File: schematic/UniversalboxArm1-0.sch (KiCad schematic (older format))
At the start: 170 parts, among them J1 USB_B_Micro, J110 Conn_01x03_Male, J120 Conn_02x04_Counter_Clockwise, J121 Conn_01x02_Male, J20 AVR-ISP-6, J50 Conn_01x14_Female, J60 Conn_01x06_Female, J61 Conn_02x08_Odd_Even, J62 Conn_02x04_Odd_Even, J90 Conn_02x03_Odd_Even, J91 Conn_02x04_Odd_Even, K90 IM01, K91 IM01, K92 IM01, K93 IM01, Q120 IRLML6402, Q20 BCX56-16, Q21 BSS138, Q22 BSS138, Q23 IRLML6402, Q24 IRLML6402, Q25 BSS138, Q50 IRLML6402, Q51 IRLML6402, Q60 BSS138, Q61 BSS138, Q62 BSS138, Q90 BSS138, Q91 BSS138, Q92 BSS138, Q93 BSS138, SW60 SW_SPST, SW61 SW_SPST, SW62 SW_SPST, SW63 SW_SPST, U1 USBLC6-2SC6, U110 MAX3221, U130 TSOP312xx, U2 LP38693MP-3.3, U20 ATtiny861A-SU, U21 REF3020, U22 MCP6542, U50 AT45DB641-S, U60 STM32L452RETx, U61 MCP65R41T-1202E, Y60 32768Hz, Y61 8MHz

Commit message: Schematic: Revision 0.9 Add worarounds for electric issues when the internal bootloader is active - bug 10. Document bug 11 - wrong signal names on PCB
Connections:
- net labels added: 330Ω, Led1Red, Led1green
- net labels removed: Led2Red, Led2green
- wire segments 765 -> 772
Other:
- note added: "B+"
- note added: "Checked for the STM32L45xxx:\nBP+: Bootloader drives this pin as pull-up\nB+: Bootloader drives this pin as output high\nBP-: Bootloader drives this pin as pull-down\nB-: Bootloader drives this pin as output low\nRP+: Bootloader and reset drives this pin as pull-up"
- note added: "LED1"
- note added: "LED2"
- note added: "Replace R53 by Diode\nTS4148 RY"
- note added: "STM32F413R"
- note added: "STM32F722R"
- note added: "STM32F730R8"
- note added: "STM32H7B0RB"
- note added: "STM32L452R"
- note added: "STM32L496R"
- note removed: "Checked for the STM32L45xxx:\nBP+: Bootloader drives this pin as pull-up\nBP-: Bootloader drives this pin as pull-down\nRP+: Bootloader and reset drives this pin as pull-up"
- note removed: "STM32F413"
- note removed: "STM32F722"
- note removed: "STM32F730"
- note removed: "STM32H7B0"
- note removed: "STM32L452"
- note removed: "STM32L496"
- moved on the sheet: C51, C69, C70, D60, D61, R53, R62, R63, R64, R65, U50, Y61

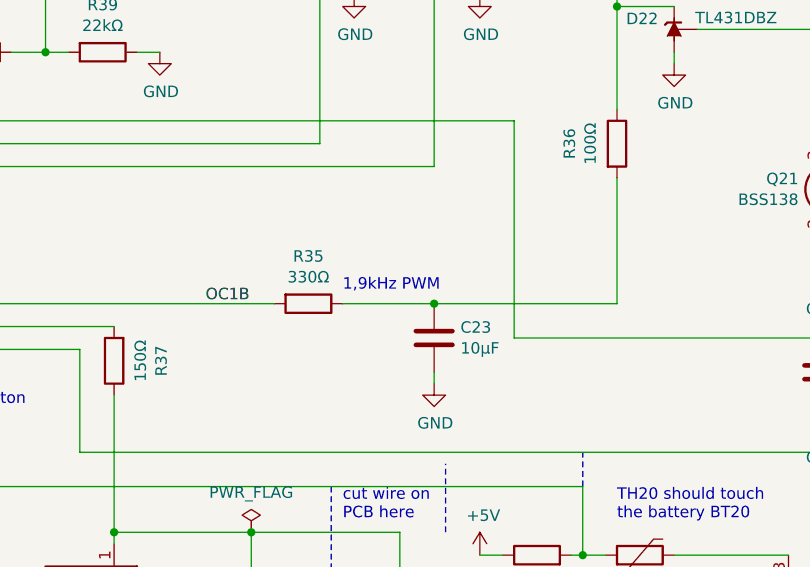
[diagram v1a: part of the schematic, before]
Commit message: Schematic: Update to 0.10
Adjust documented PWM frequency to the one used by the firmware
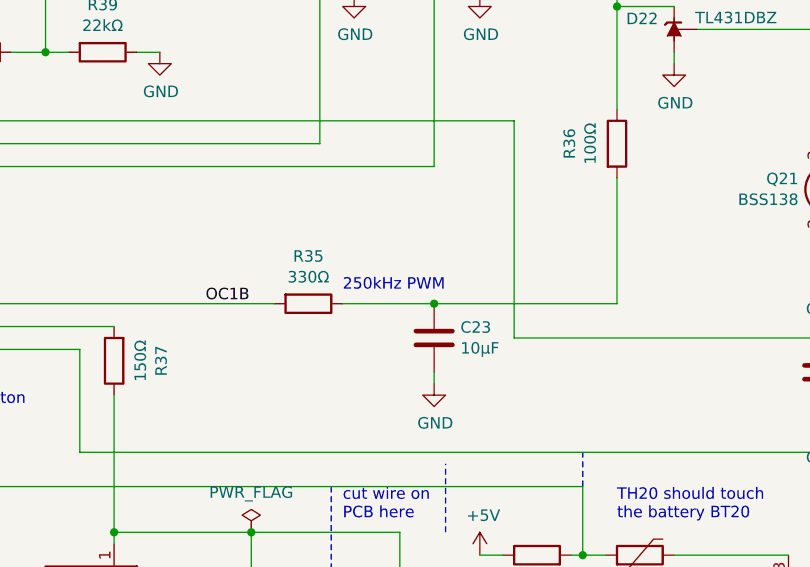
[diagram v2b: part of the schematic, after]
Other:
- note added: "250kHz PWM"
- note removed: "1,9kHz PWM"
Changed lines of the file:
@@
 Sheet 1 1
 Title ""
-Date "2022-02-20"
-Rev "0.9"
+Date "2022-08-21"
+Rev "0.10"
 Comp ""
 Comment1 ""
@@
 	5500 5750 5500 5800
 Text Notes 5100 5400 0    50   ~ 0
-1,9kHz PWM
+250kHz PWM
 $Comp
 L Device:D_Schottky D1

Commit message: Schematic: Version 0.11, update parts, reroute LCD reset
LCD reset is now connected to PC2, this allows I2C on PC0 and PC1 to be used.
R34 has been reduced to 470Ohm.
Q61 and Q62 are replaced by IRLML6344 to switch higher currents.
R55 has been added. This should allow to access the flash with 4MHz instead of 250kHz.

Measurements on R55 show the required low level of 1V is now reached within 250ns.
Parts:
- Q61, Q62: value BSS138 -> IRLML6344
- R34: value 1kΩ -> 470Ω
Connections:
- net labels added: 4700Ω
- wire segments 772 -> 775
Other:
- note added: "Pull down required\nfor >250kHz SPI"
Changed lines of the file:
@@
 Sheet 1 1
 Title ""
-Date "2022-08-21"
-Rev "0.10"
+Date "2022-10-30"
+Rev "0.11"
 Comp ""
 Comment1 ""
@@
 P 1850 7050
 F 0 "R34" V 1643 7050 50  0000 C CNN
-F 1 "1kΩ" V 1734 7050 50  0000 C CNN
+F 1 "470Ω" V 1734 7050 50  0000 C CNN
 F 2 "Resistor_SMD:R_0805_2012Metric_Pad1.15x1.40mm_HandSolder" V 1780 7050 50  0001 C CNN
 F 3 "~" H 1850 7050 50  0001 C CNN
@@
 Spi1Mosi
 Connection ~ 6800 11800
-Text Notes 3100 11700 0    50   ~ 0
+Text Notes 2700 11700 0    50   ~ 0
 BootPin
 Wire Wire Line
@@
 P 14600 13900
 F 0 "Q61" H 14805 13946 50  0000 L CNN
-F 1 "BSS138" H 14805 13855 50  0000 L CNN
+F 1 "IRLML6344" H 14805 13855 50  0000 L CNN
 F 2 "Package_TO_SOT_SMD:SOT-23" H 14800 13825 50  0001 L CIN
 F 3 "https://www.fairchildsemi.com/datasheets/BS/BSS138.pdf" H 14600 13900 50  0001 L CNN
@@
 P 16000 13900
 F 0 "Q62" H 16205 13946 50  0000 L CNN
-F 1 "BSS138" H 16205 13855 50  0000 L CNN
+F 1 "IRLML6344" H 16205 13855 50  0000 L CNN
 F 2 "Package_TO_SOT_SMD:SOT-23" H 16200 13825 50  0001 L CIN
 F 3 "https://www.fairchildsemi.com/datasheets/BS/BSS138.pdf" H 16000 13900 50  0001 L CNN
@@
 Wire Wire Line
 	9000 8800 9250 8800
-Wire Wire Line
-	9000 9200 9000 9900
 Connection ~ 9000 9900
 Wire Wire Line
@@
 	3100 12400 3750 12400
 Wire Wire Line
-	3100 12300 3750 12300
-Wire Wire Line
 	3050 12200 3050 9900
 Wire Wire Line
@@
 Wire Notes Line width 12 rgb(255, 0, 0)
 	10800 11800 10800 11450
-Text Notes 11100 11400 0    50   ~ 0
+Text Notes 11000 11600 0    50   ~ 0
 Replace R53 by Diode\nTS4148 RY
 $Comp
@@
 Text Notes 11750 14300 0    50   ~ 0
 LED2
+$Comp
+L Device:R #R55
+U 1 1 6369378A
+P 11200 10950
+F 0 "#R55" V 10993 10950 50  0000 C CNN
+F 1 "4700Ω" V 11084 10950 50  0000 C CNN
+F 2 "Resistor_SMD:R_0805_2012Metric_Pad1.15x1.40mm_HandSolder" V 11130 10950 50  0001 C CNN
+F 3 "~" H 11200 10950 50  0001 C CNN
+	1    11200 10950
+	0    -1   -1   0
+$EndComp
+Wire Wire Line
+	11050 10950 10200 10950
+Wire Wire Line
+	10200 10950 10200 11300
+$Comp
+L power:GND #PWR0109
+U 1 1 6372F3E6
+P 11500 10950
+F 0 "#PWR0109" H 11500 10700 50  0001 C CNN
+F 1 "GND" H 11505 10777 50  0000 C CNN
+F 2 "" H 11500 10950 50  0001 C CNN
+F 3 "" H 11500 10950 50  0001 C CNN
+	1    11500 10950
+	1    0    0    -1
+$EndComp
+Wire Wire Line
+	11500 10950 11350 10950
+Text Notes 11100 10850 0    50   ~ 0
+Pull down required\nfor >250kHz SPI
+Wire Wire Line
+	9000 9200 9000 9900
+Wire Wire Line
+	3100 12300 3750 12300
+Wire Bus Line
+	9000 9600 3350 9600
+Wire Bus Line
+	3350 9600 3350 12300
 $EndSCHEMATC

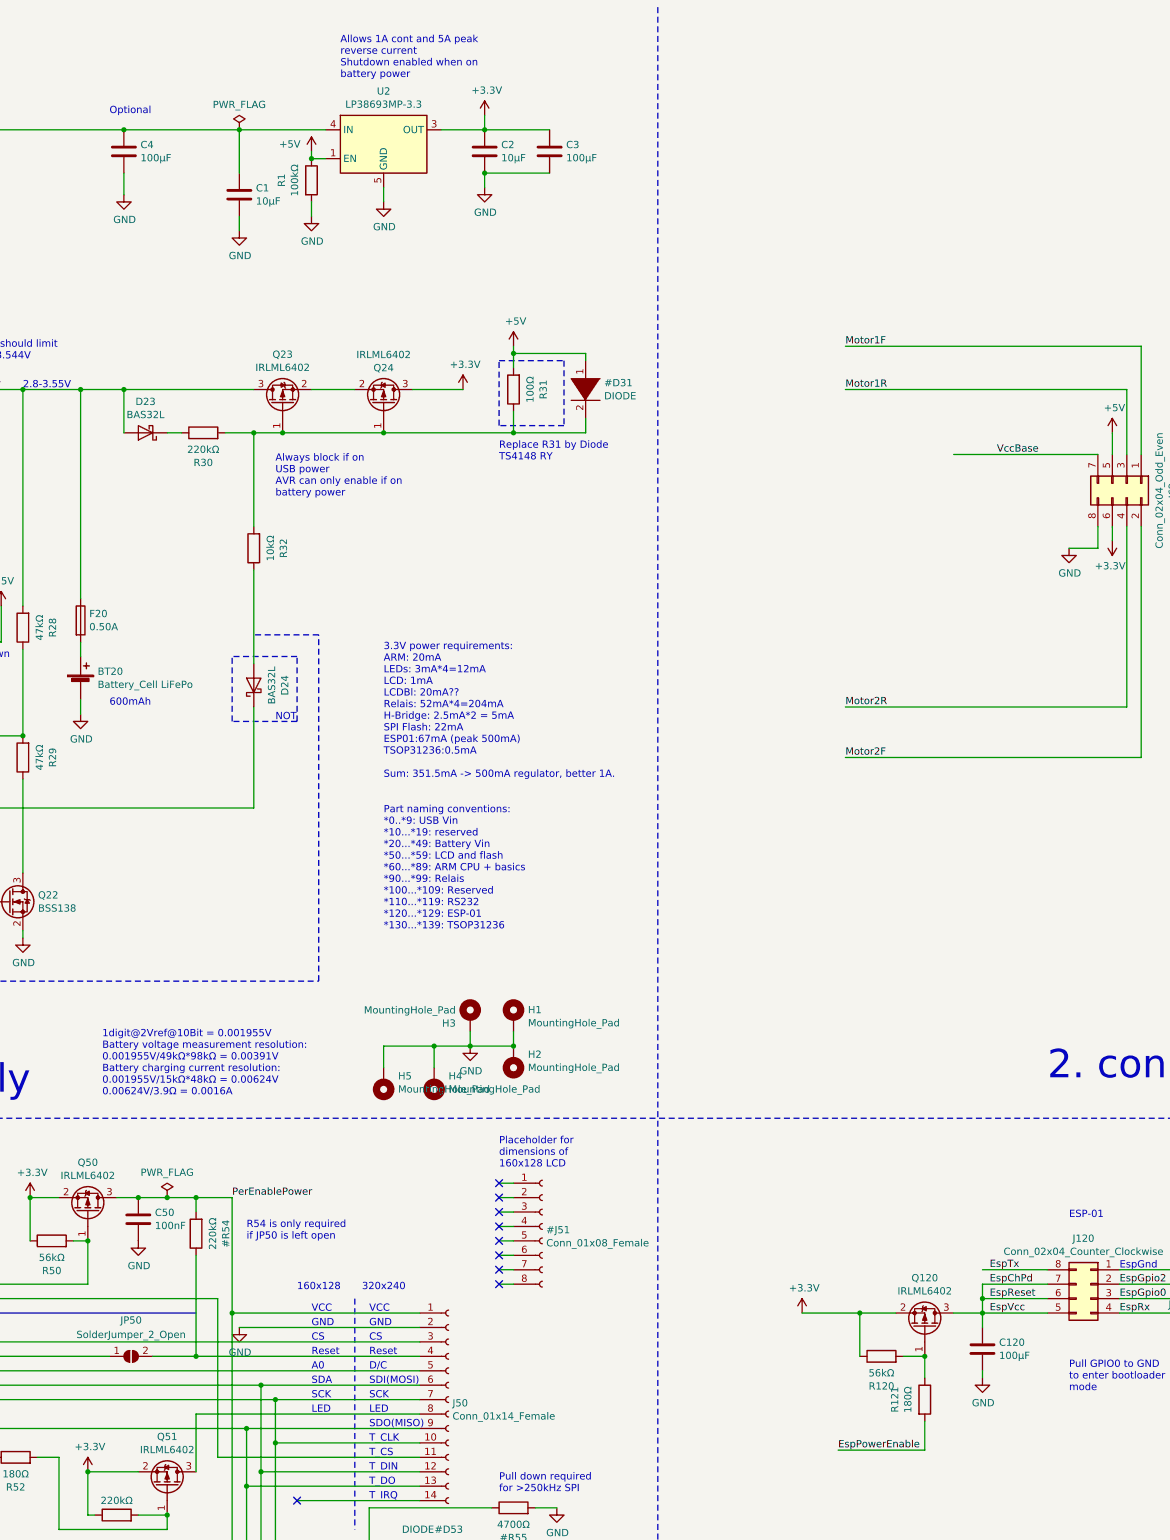
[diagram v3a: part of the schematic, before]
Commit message: Schematic: Fix power surge of ESP-01 module
Add C121, reduce C120. Make C4 not recommend.
Schematic vesion 0.12.
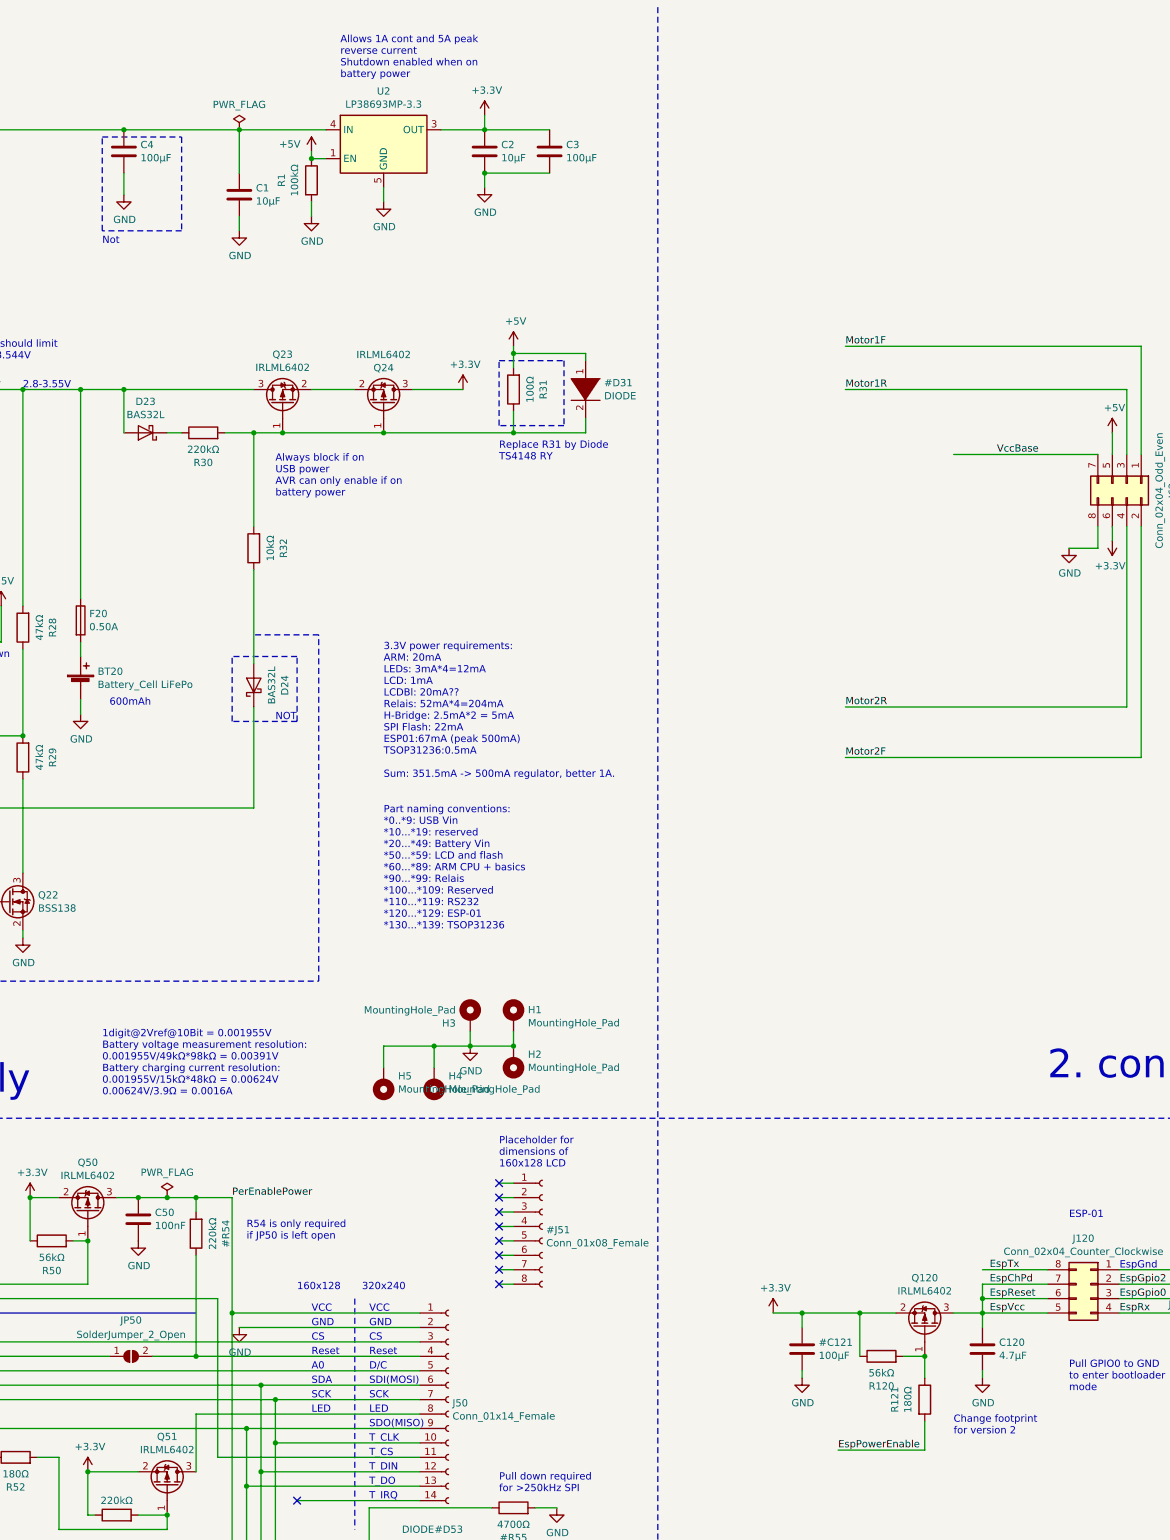
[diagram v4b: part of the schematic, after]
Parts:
- C120: value 100µF -> 4.7µF
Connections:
- net labels added: 100µF
- wire segments 775 -> 778
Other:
- note added: "Change footprint\nfor version 2"
- note added: "Not"
- note removed: "Optional"
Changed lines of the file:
@@
 Sheet 1 1
 Title ""
-Date "2022-10-30"
-Rev "0.11"
+Date "2023-04-01"
+Rev "0.12"
 Comp ""
 Comment1 ""
@@
 P 14450 9850
 F 0 "C120" H 14565 9896 50  0000 L CNN
-F 1 "100µF" H 14565 9805 50  0000 L CNN
+F 1 "4.7µF" H 14565 9805 50  0000 L CNN
 F 2 "Capacitor_SMD:C_1206_3216Metric_Pad1.33x1.80mm_HandSolder" H 14488 9700 50  0001 C CNN
 F 3 "~" H 14450 9850 50  0001 C CNN
@@
 Connection ~ 13600 9600
 Wire Wire Line
-	13600 9600 13200 9600
-Wire Wire Line
 	13900 9900 14050 9900
 Wire Wire Line
@@
 L power:+3.3V #PWR0193
 U 1 1 6366C390
-P 13200 9600
-F 0 "#PWR0193" H 13200 9450 50  0001 C CNN
-F 1 "+3.3V" H 13215 9773 50  0000 C CNN
-F 2 "" H 13200 9600 50  0001 C CNN
-F 3 "" H 13200 9600 50  0001 C CNN
-	1    13200 9600
+P 13000 9600
+F 0 "#PWR0193" H 13000 9450 50  0001 C CNN
+F 1 "+3.3V" H 13015 9773 50  0000 C CNN
+F 2 "" H 13000 9600 50  0001 C CNN
+F 3 "" H 13000 9600 50  0001 C CNN
+	1    13000 9600
 	1    0    0    -1
 $EndComp
@@
 Wire Wire Line
 	8500 1400 9300 1400
-Text Notes 8400 1300 0    50   ~ 0
-Optional
+Text Notes 8350 2200 0    50   ~ 0
+Not
 $Comp
 L power:GND #PWR0108
@@
 Wire Bus Line
 	3350 9600 3350 12300
+Wire Notes Line rgb(255, 0, 0)
+	8350 1450 8900 1450
+Wire Notes Line rgb(255, 0, 0)
+	8900 1450 8900 2100
+Wire Notes Line rgb(255, 0, 0)
+	8900 2100 8350 2100
+Wire Notes Line rgb(255, 0, 0)
+	8350 2100 8350 1450
+$Comp
+L Device:C #C121
+U 1 1 64400EB2
+P 13200 9850
+F 0 "#C121" H 13315 9896 50  0000 L CNN
+F 1 "100µF" H 13315 9805 50  0000 L CNN
+F 2 "Capacitor_SMD:C_1206_3216Metric_Pad1.33x1.80mm_HandSolder" H 13238 9700 50  0001 C CNN
+F 3 "~" H 13200 9850 50  0001 C CNN
+	1    13200 9850
+	1    0    0    -1
+$EndComp
+Text Notes 14250 10450 0    50   ~ 0
+Change footprint\nfor version 2
+Wire Wire Line
+	13000 9600 13200 9600
+Connection ~ 13200 9600
+Wire Wire Line
+	13200 9600 13600 9600
+$Comp
+L power:GND #PWR?
+U 1 1 6454A531
+P 13200 10050
+F 0 "#PWR?" H 13200 9800 50  0001 C CNN
+F 1 "GND" H 13205 9877 50  0000 C CNN
+F 2 "" H 13200 10050 50  0001 C CNN
+F 3 "" H 13200 10050 50  0001 C CNN
+	1    13200 10050
+	1    0    0    -1
+$EndComp
+Wire Wire Line
+	13200 9700 13200 9600
+Wire Wire Line
+	13200 10050 13200 10000
 $EndSCHEMATC
